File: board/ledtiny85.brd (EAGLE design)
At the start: 37.1 x 27.3 mm, 19 parts, among them J3 AVR_SPI_PRG_6PTH, U1 Tiny85-20-SMT

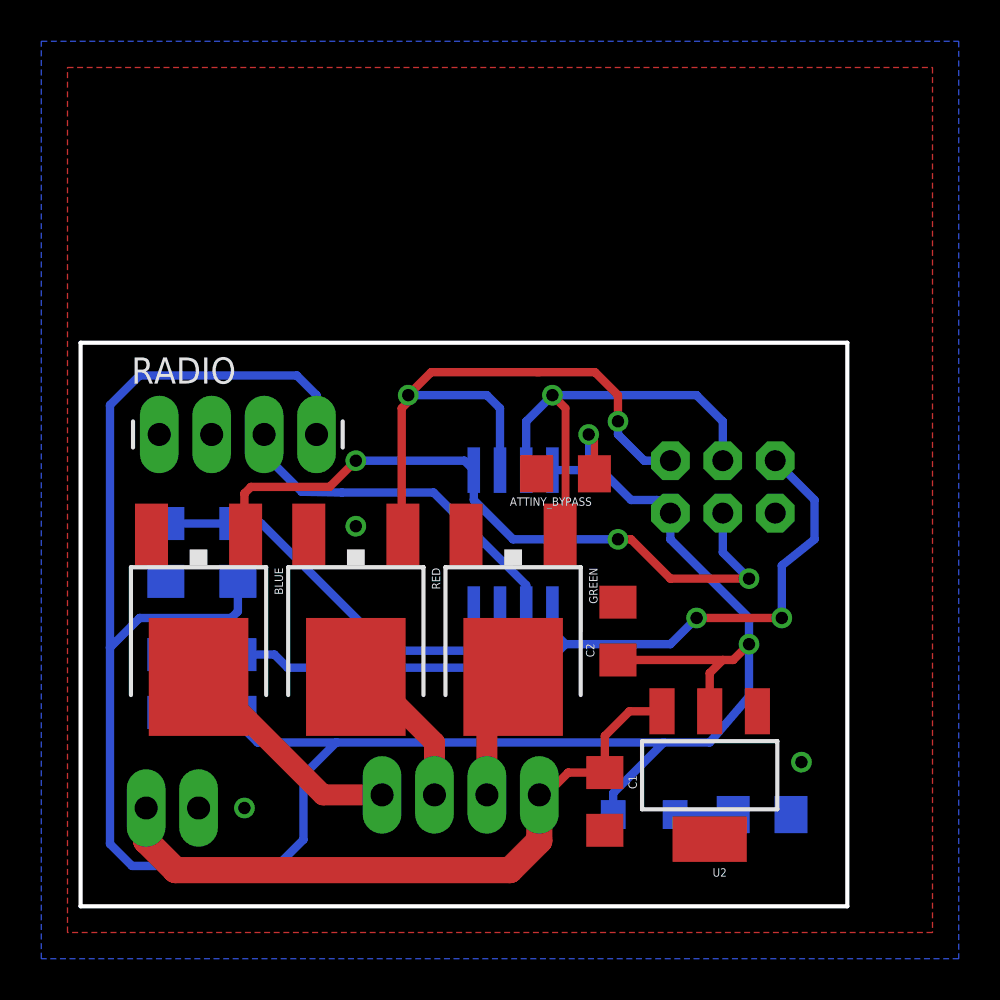
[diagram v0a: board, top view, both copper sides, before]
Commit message: Add OSHW logo to board
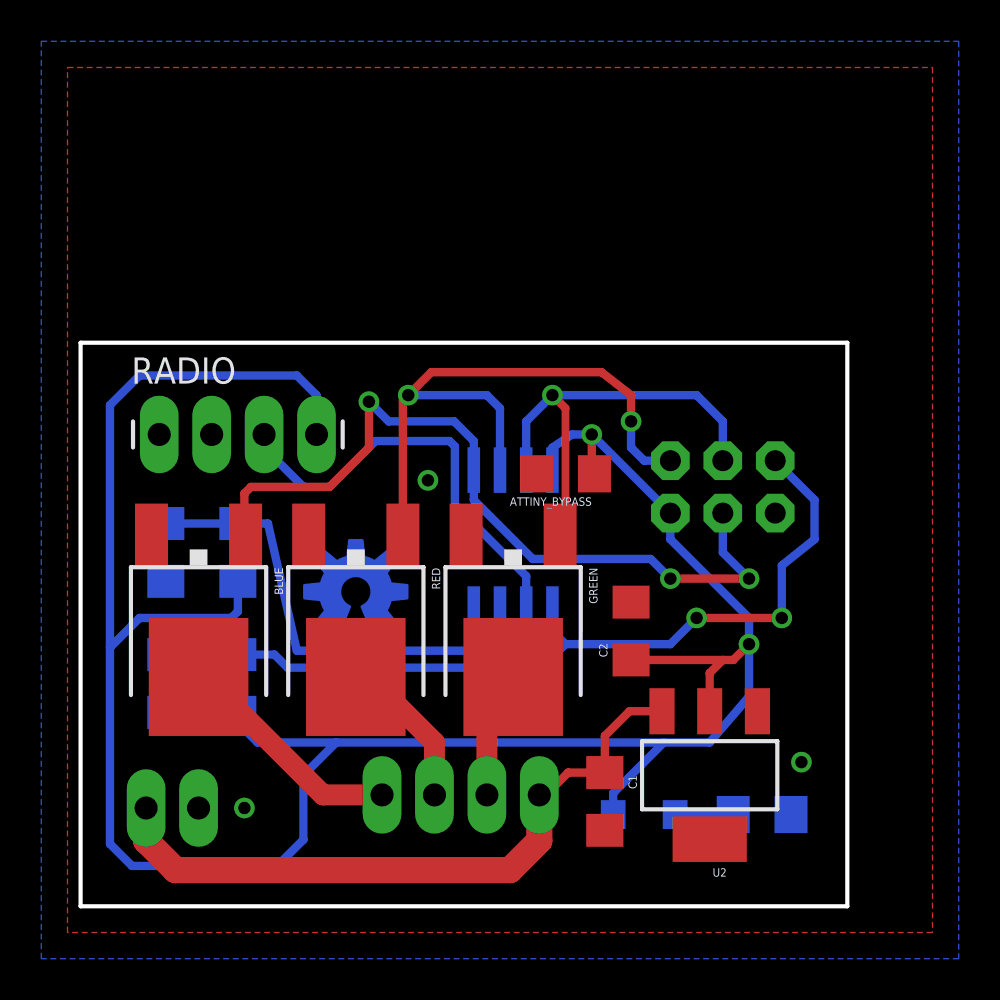
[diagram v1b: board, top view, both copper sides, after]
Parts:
- added U$2: (no value), SparkFun-Aesthetics:OSHW-LOGO-M_COPPER
- moved C2 0.64 mm to (27.0, 13.7)
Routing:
- net PB0: track 34.0 -> 38.5 mm
- net PB3: track 17.4 -> 21.0 mm
- net PB4: track 20.6 -> 23.0 mm
- net GREEN: track 8.54 -> 7.98 mm
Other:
- board text added: "Willie Zhu"

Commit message: Make vias bigger
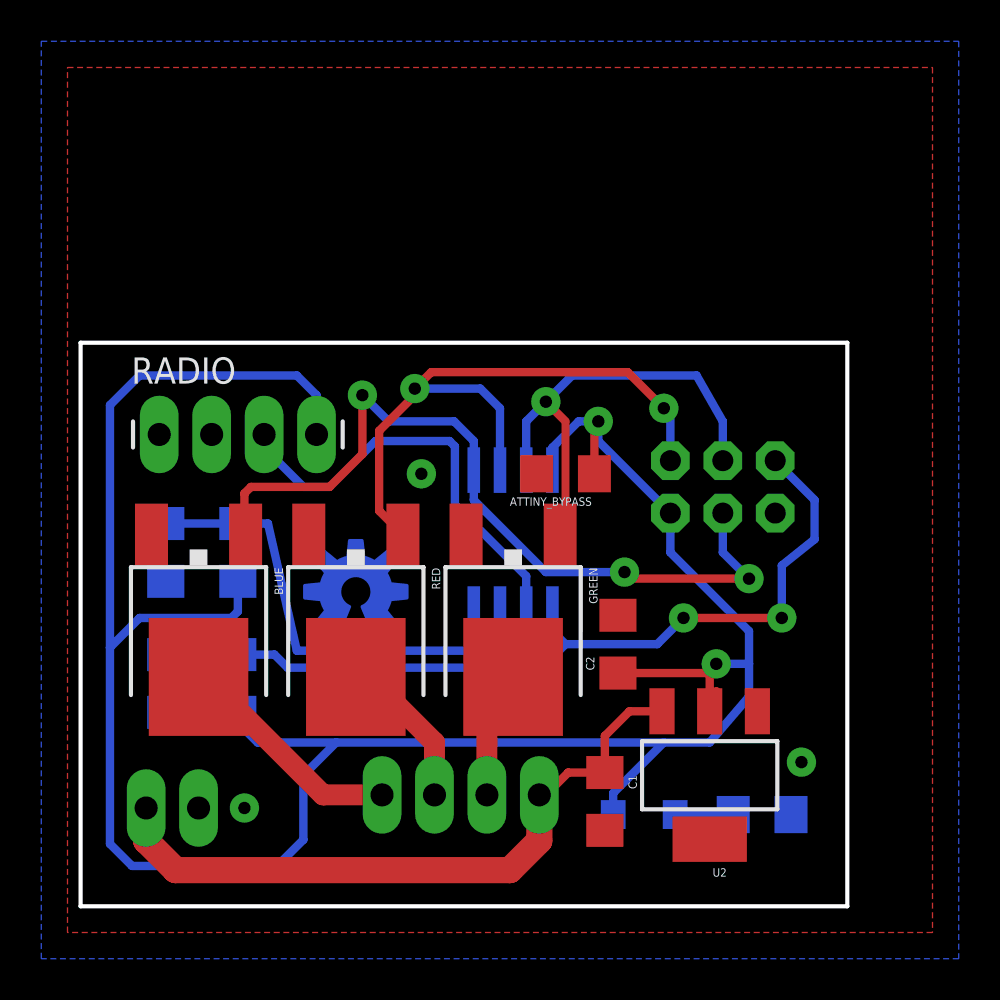
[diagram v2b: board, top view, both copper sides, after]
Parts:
- moved C2 0.90 mm to (26.4, 13.0)
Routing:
- net 3.3V: track 119.7 -> 123.0 mm
- net PB2: track 22.0 -> 22.9 mm
- net PB1: track 30.9 -> 31.6 mm
- net PB0: track 38.5 -> 39.2 mm

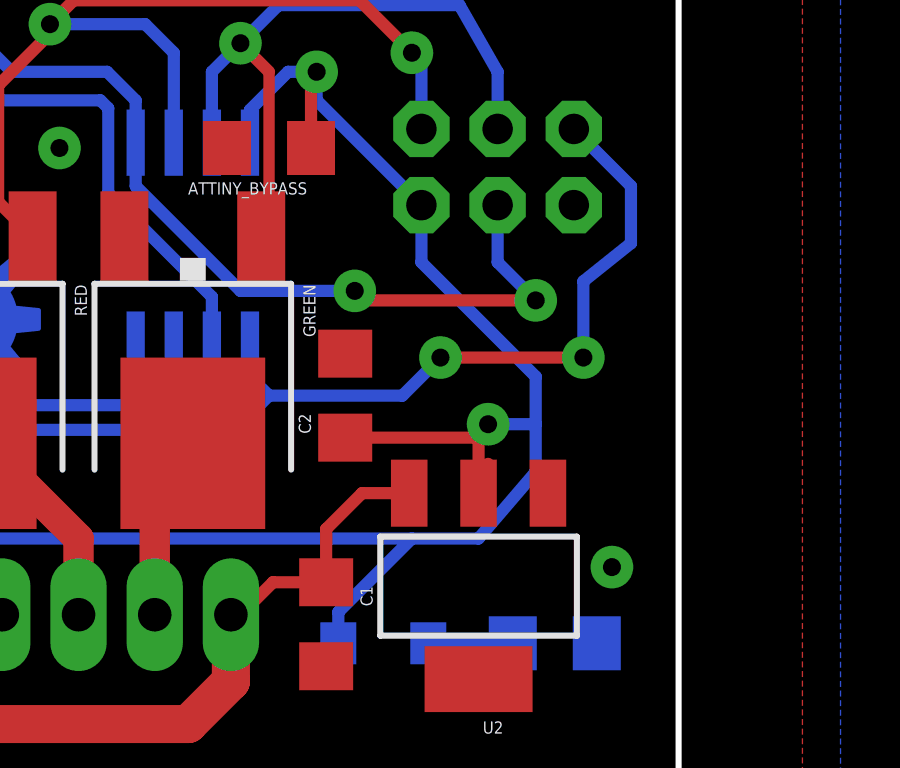
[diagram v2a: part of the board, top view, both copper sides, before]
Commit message: Fix broken ground pour
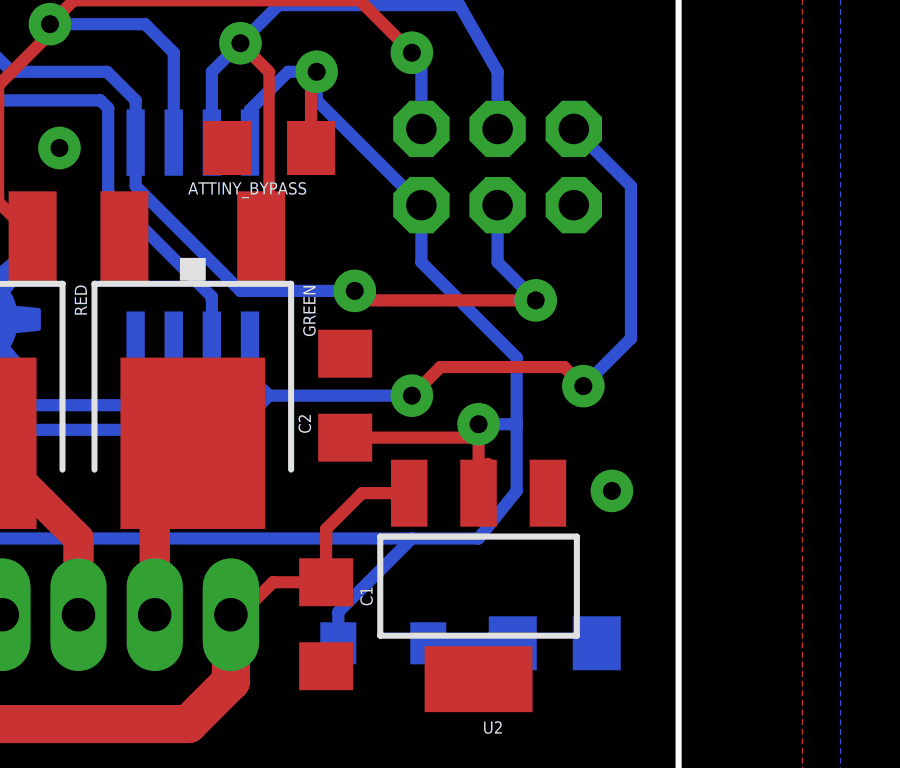
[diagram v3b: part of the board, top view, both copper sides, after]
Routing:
- net 3.3V: track 123.0 -> 121.9 mm
- net PB5: track 42.2 -> 43.2 mm
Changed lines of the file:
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@@
 </polygon>
 <contactref element="R5" pad="2"/>
-<via x="35.2425" y="7.3025" extent="1-16" drill="0.6" diameter="1.4224" shape="square"/>
+<via x="35.2425" y="9.8425" extent="1-16" drill="0.6" diameter="1.4224" shape="square"/>
 <via x="8.255" y="5.08" extent="1-16" drill="0.6" diameter="1.4224" shape="square"/>
 <contactref element="ATTINY_BYPASS" pad="2"/>
@@
 <contactref element="R3" pad="1"/>
 <contactref element="POWER_LED" pad="A"/>
-<wire x1="32.7025" y1="12.065" x2="32.7025" y2="10.4775" width="0.4064" layer="16"/>
-<wire x1="32.7025" y1="12.065" x2="32.7025" y2="13.6525" width="0.4064" layer="16"/>
-<wire x1="32.7025" y1="10.4775" x2="30.7975" y2="8.255" width="0.4064" layer="16"/>
-<wire x1="32.7025" y1="13.6525" x2="28.8925" y2="17.4625" width="0.4064" layer="16"/>
+<wire x1="32.0675" y1="12.065" x2="32.0675" y2="9.8425" width="0.4064" layer="16"/>
+<wire x1="32.0675" y1="12.065" x2="32.0675" y2="14.2875" width="0.4064" layer="16"/>
+<wire x1="32.0675" y1="9.8425" x2="30.7975" y2="8.255" width="0.4064" layer="16"/>
+<wire x1="32.0675" y1="14.2875" x2="28.8925" y2="17.4625" width="0.4064" layer="16"/>
 <wire x1="28.8925" y1="19.3675" x2="28.8925" y2="17.4625" width="0.4064" layer="16"/>
 <wire x1="1.7399" y1="12.8524" x2="1.7399" y2="24.5999" width="0.4064" layer="16"/>
@@
 <wire x1="31.115" y1="10.0838" x2="30.7975" y2="9.7663" width="0.4064" layer="1"/>
 <wire x1="31.115" y1="10.0838" x2="31.115" y2="10.7442" width="0.4064" layer="1"/>
-<via x="31.115" y="12.065" extent="1-16" drill="0.6" diameter="1.4224" shape="square"/>
-<wire x1="30.7975" y1="9.7663" x2="30.7975" y2="11.7475" width="0.4064" layer="1"/>
-<wire x1="31.115" y1="12.065" x2="30.7975" y2="11.7475" width="0.4064" layer="1"/>
-<wire x1="31.115" y1="12.065" x2="32.7025" y2="12.065" width="0.4064" layer="16"/>
+<via x="30.7975" y="12.065" extent="1-16" drill="0.6" diameter="1.4224" shape="square"/>
+<wire x1="30.7975" y1="9.7663" x2="30.7975" y2="12.065" width="0.4064" layer="1"/>
+<wire x1="30.7975" y1="12.065" x2="32.0675" y2="12.065" width="0.4064" layer="16"/>
 <wire x1="26.3525" y1="11.6175" x2="30.6675" y2="11.6175" width="0.4064" layer="1"/>
-<wire x1="30.6675" y1="11.6175" x2="31.115" y2="12.065" width="0.4064" layer="1"/>
+<wire x1="30.6675" y1="11.6175" x2="30.7975" y2="12.065" width="0.4064" layer="1"/>
 <wire x1="25.4" y1="22.86" x2="25.4" y2="23.8125" width="0.4064" layer="16"/>
 <wire x1="25.4" y1="22.86" x2="28.8925" y2="19.3675" width="0.4064" layer="16"/>
@@
 <contactref element="R4" pad="1"/>
 <wire x1="33.9725" y1="21.9075" x2="35.8775" y2="20.0025" width="0.4064" layer="16"/>
-<wire x1="35.8775" y1="20.0025" x2="35.8775" y2="18.0975" width="0.4064" layer="16"/>
-<wire x1="35.8775" y1="18.0975" x2="34.29" y2="16.8275" width="0.4064" layer="16"/>
-<wire x1="34.29" y1="16.8275" x2="34.29" y2="14.2875" width="0.4064" layer="16"/>
-<via x="34.29" y="14.2875" extent="1-16" drill="0.6" diameter="1.4224" shape="square"/>
-<wire x1="34.29" y1="14.2875" x2="29.5275" y2="14.2875" width="0.4064" layer="1"/>
-<via x="29.5275" y="14.2875" extent="1-16" drill="0.6" diameter="1.4224" shape="square"/>
-<wire x1="29.5275" y1="14.2875" x2="28.2575" y2="13.0175" width="0.4064" layer="16"/>
-<wire x1="23.8125" y1="13.0175" x2="28.2575" y2="13.0175" width="0.4064" layer="16"/>
+<wire x1="35.8775" y1="20.0025" x2="35.8775" y2="14.9225" width="0.4064" layer="16"/>
+<wire x1="35.8775" y1="14.9225" x2="34.29" y2="13.335" width="0.4064" layer="16"/>
+<via x="34.29" y="13.335" extent="1-16" drill="0.6" diameter="1.4224" shape="square"/>
+<via x="28.575" y="13.0175" extent="1-16" drill="0.6" diameter="1.4224" shape="square"/>
+<wire x1="23.8125" y1="13.0175" x2="28.575" y2="13.0175" width="0.4064" layer="16"/>
 <wire x1="23.8125" y1="13.0175" x2="23.1775" y2="13.6525" width="0.4064" layer="16"/>
 <wire x1="23.1775" y1="13.6525" x2="23.1775" y2="14.7193" width="0.4064" layer="16"/>
@@
 <wire x1="7.9375" y1="12.5125" x2="9.7125" y2="12.5125" width="0.4064" layer="16"/>
 <wire x1="9.7125" y1="12.5125" x2="10.3475" y2="11.8775" width="0.4064" layer="16"/>
+<wire x1="28.575" y1="13.0175" x2="29.5275" y2="13.97" width="0.4064" layer="1"/>
+<wire x1="29.5275" y1="13.97" x2="33.655" y2="13.97" width="0.4064" layer="1"/>
+<wire x1="33.655" y1="13.97" x2="34.29" y2="13.335" width="0.4064" layer="1"/>
 </signal>
 <signal name="N$6">
